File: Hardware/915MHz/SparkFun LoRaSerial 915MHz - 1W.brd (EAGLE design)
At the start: 50.8 x 27.4 mm, 94 parts, among them J1 QWIIC_RIGHT_ANGLE, J3 USB C, J4 JTAG, Q1 20V/0.2A/8MHz/1.2Ω/1Vth, Q2 20V/0.2A/8MHz/1.2Ω/1Vth, U2 ATSAMD21G-A, U3 AP2112K-3.3, U4 E19-915M30S, Y1 32.768kHz

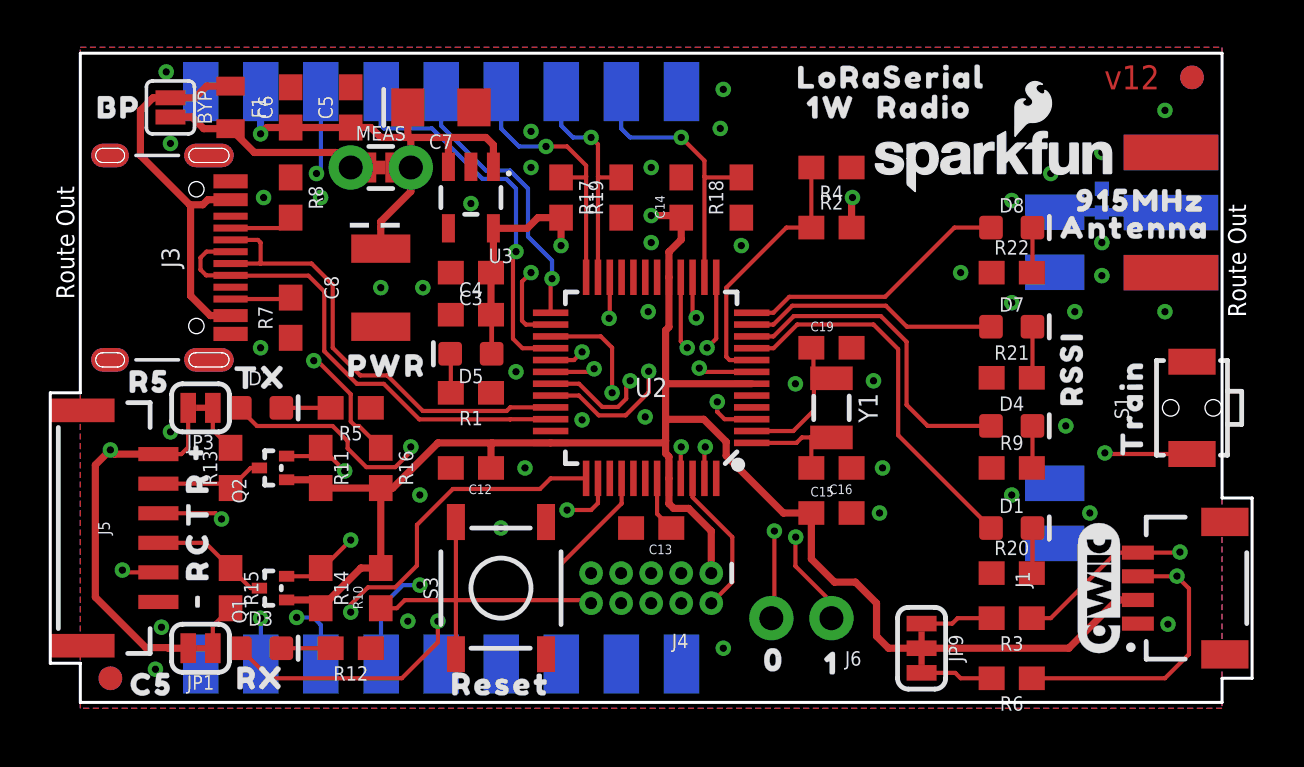
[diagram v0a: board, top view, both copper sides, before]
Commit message: Add RSSI LED drivers. v13
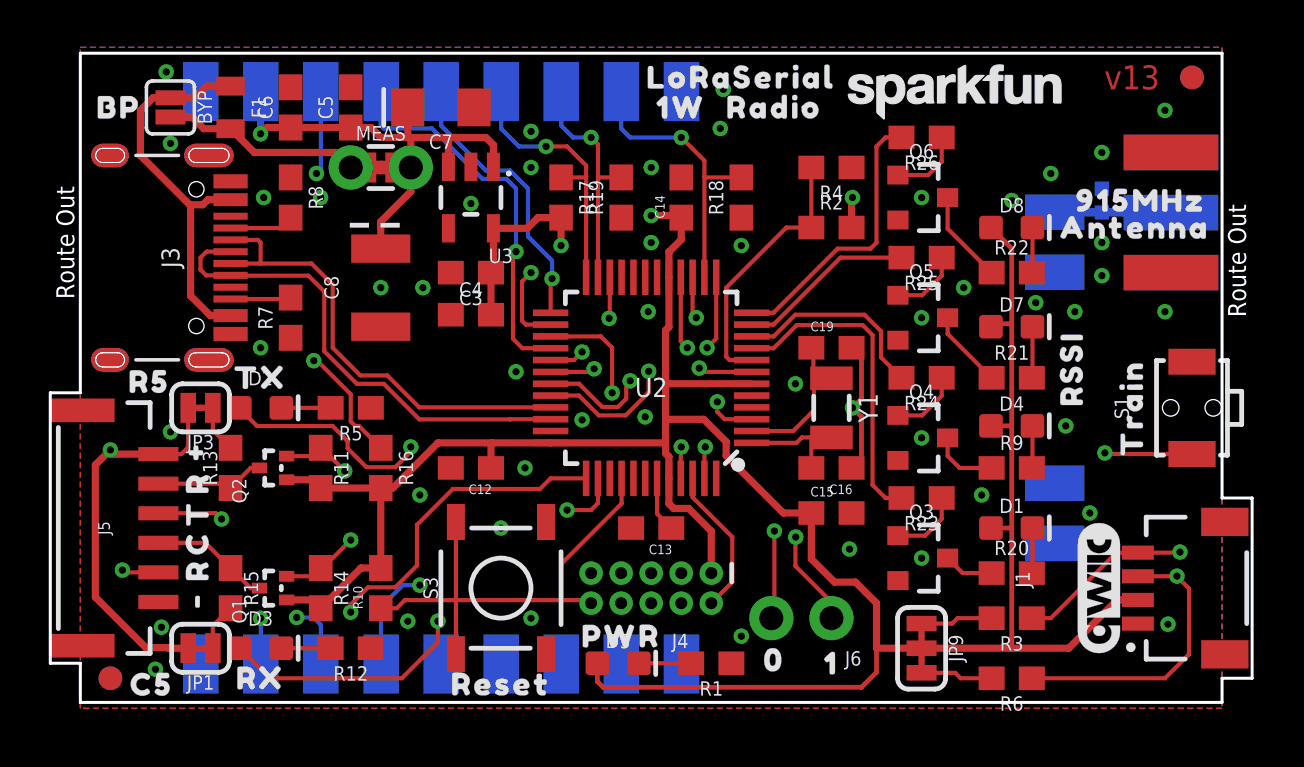
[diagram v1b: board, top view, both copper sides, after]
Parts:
- added Q3, Q4, Q5, Q6: 600mA/40V, SparkFun-DiscreteSemi:SOT23-3
- added R23, R24, R25, R26: 1k, SparkFun-Resistors:0603
- LOGO5: value SFE_LOGO_NAME_FLAME10_MM -> SFE_LOGO_NAME9_MM; device SparkFun-Aesthetics:SFE_LOGO_NAME_FLAME_10MM -> SparkFun-Aesthetics:SFE_LOGO_NAME_9MM
- R20, R21, R22, R9: value 0 -> 220
- U4: device SparkFun-RF:E19-915MS1W -> SparkFun-RF:E19-915M30S
- moved R1 15.3 mm to (27.9, 1.91)
- moved U$7 15.1 mm to (24.1, 3.05)
- moved D5 14.5 mm to (24.0, 1.91), turned to 0 degrees
- moved U$1 6.35 mm to (26.7, 25.4)
- moved U$18 6.35 mm to (29.2, 26.7)
- moved U$5 6.35 mm to (30.6, 25.4)
- moved LOGO5 3.36 mm to (38.2, 26.2)
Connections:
- new net N$12: Q3.3, R20.1
- new net N$13: Q3.1, R23.1
- new net N$14: Q4.3, R9.1
- new net N$15: Q4.1, R24.1
- new net N$16: Q5.3, R21.1
- new net N$17: Q5.1, R25.1
- new net N$18: Q6.3, R22.1
- new net N$19: Q6.1, R26.1
- net 3.3V: now also D1.A, D4.A, D7.A, D8.A
- net A3/RSSI1: now also R23.2; no longer D1.A
- net A4/RSSI2: now also R24.2; no longer D4.A
- net D8/RSSI3: now also R25.2; no longer D7.A
- net D9/RSSI4: now also R26.2; no longer D8.A
- net GND: now also Q3.2, Q4.2, Q5.2, Q6.2; no longer R20.1, R21.1, R22.1, R9.1
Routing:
- net 3.3V: track 98.9 -> 132.3 mm
- net GND: track 0.00 -> 5.74 mm, vias 45 -> 49
- net A4/RSSI2: track 14.0 -> 8.46 mm
- net N$18: track 0.00 -> 3.95 mm
- net N$16: track 0.00 -> 3.31 mm
- net D8/RSSI3: track 10.8 -> 7.50 mm
- net N$19: track 0.00 -> 3.10 mm
- net N$13: track 0.00 -> 3.03 mm
- net N$17: track 0.00 -> 2.95 mm
- net N$15: track 0.00 -> 2.95 mm
- net N$14: track 0.00 -> 2.83 mm
- net A3/RSSI1: track 16.2 -> 13.5 mm
- net N$12: track 0.00 -> 2.12 mm
- net N$7: track 1.66 -> 2.21 mm
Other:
- board text added: "v13"
- board text removed: "v12"

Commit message: Add TPs, GND stitching, sch cosmetic cleanup.
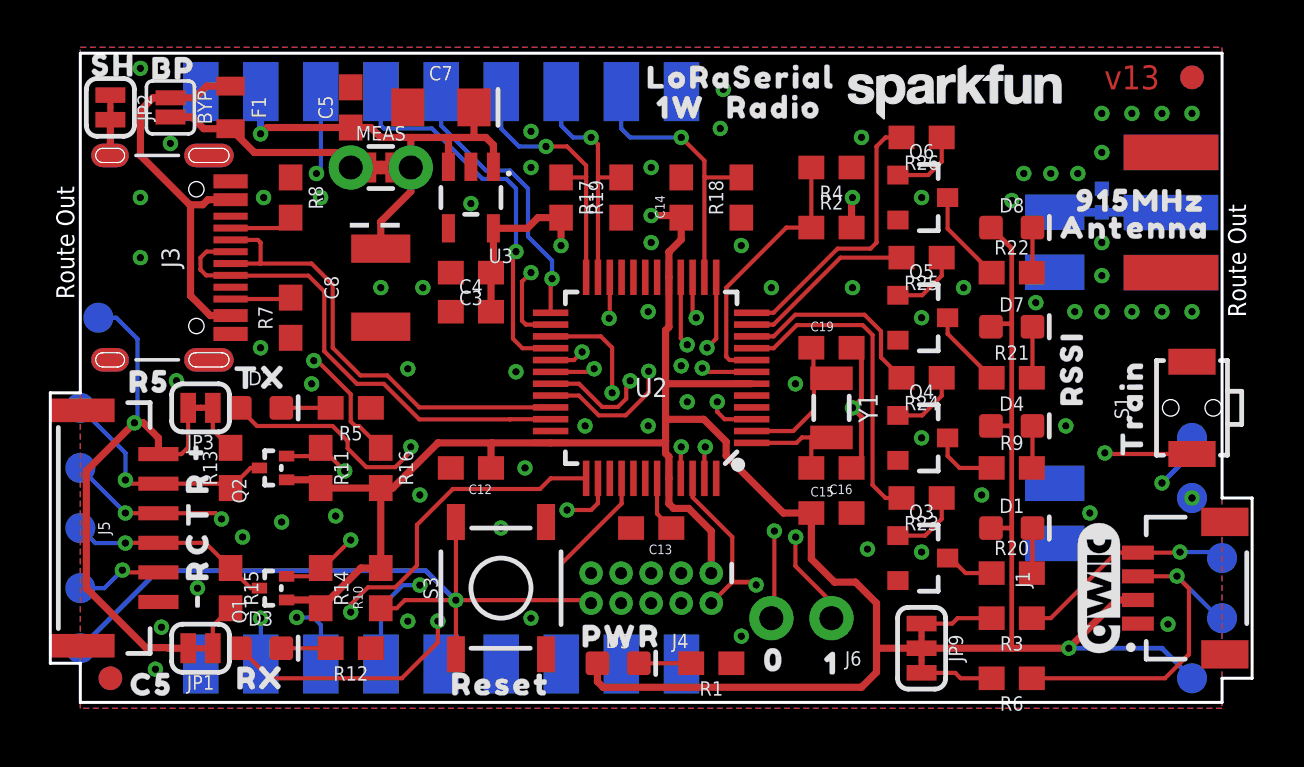
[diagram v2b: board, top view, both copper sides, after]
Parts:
- removed C6: 0.1uF, SparkFun-Capacitors:0603
- added JP2: (no value), SparkFun-Jumpers:SMT-JUMPER_2_NC_TRACE_SILK
- added TP1, TP10, TP11, TP2, TP3, TP4, TP5, TP6, TP7, TP8, TP9: (no value), SparkFun-Connectors:PAD.03X.05
- added U$23: (no value), output:SH0
- C5: value 0.22uF -> 1.0uF
- LOGO2: value SFE_LOGO_NAME_FLAME.1_INCH -> SFE_LOGO_NAME_FLAME9_MM; device SparkFun-Aesthetics:SFE_LOGO_NAME_FLAME_.1 -> SparkFun-Aesthetics:SFE_LOGO_NAME_FLAME_9MM
- moved U$8 2.84 mm to (5.21, 27.1)
- moved LOGO4 1.94 mm to (44.5, 25.4), turned to 90 degrees
- moved C4 0.13 mm to (17.8, 16.8)
- turned C7 to 0 degrees
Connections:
- new net N$20: J3.SHLD1, J3.SHLD2, J3.SHLD3, J3.SHLD4, J3.SHLD5, J3.SHLD6, J3.SHLD7, J3.SHLD8, JP2.2
- net 3.3V: now also TP1.1
- net 5V: now also TP2.1; no longer C6.1
- net CTS-I_HV: now also TP6.1
- net D20/SDA: now also TP10.1
- net D21/SCL: now also TP11.1
- net D38/RTS-O: now also TP9.1
- net GND: now also JP2.1; no longer C6.2
- net RX-I_HV: now also TP7.1
- net SAMD_!RESET!: now also TP5.1
- net SWCLK: now also TP4.1
- net SWDIO: now also TP3.1
- net TX-O: now also TP8.1
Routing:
- net SWDIO: track 6.34 -> 35.2 mm, vias 0 -> 2
- net SWCLK: track 12.5 -> 36.0 mm, vias 1 -> 2
- net SAMD_!RESET!: track 20.9 -> 38.6 mm, vias 0 -> 1
- net 5V: track 59.6 -> 65.6 mm
- net 3.3V: track 132.3 -> 137.9 mm, vias 3 -> 4
- net RX-I_HV: track 4.70 -> 10.00 mm, vias 0 -> 1
- net TX-O: track 31.9 -> 36.0 mm, vias 2 -> 3
- net CTS-I_HV: track 5.06 -> 8.63 mm, vias 0 -> 1
- net D38/RTS-O: track 33.6 -> 36.6 mm
- net D20/SDA: track 45.8 -> 47.7 mm
- net D21/SCL: track 41.5 -> 43.4 mm
- net N$20: track 0.00 -> 1.52 mm
- net GND: vias 49 -> 70

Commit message: v13 - panel files.
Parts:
- removed BYP: JUMPER-SMT_2_NO_SILK, SparkFun-Jumpers:SMT-JUMPER_2_NO_SILK
- removed MEAS: JUMPER-COMBO_2_NC_TRACE, SparkFun-Jumpers:COMBO-JUMPER_2_NC_TRACE
- removed U$8: (no value), output:BP0
- added D9: 3A/10V/280mV, SparkFun-DiscreteSemi:SOD-323
- added Q7: (no value), SparkFun-DiscreteSemi:SOT363_PHILIPS
- added Q8: 20V/4.2A/52mΩ/1.4W, SparkFun-DiscreteSemi:SOT23-3
- added R27: 100k, SparkFun-Resistors:0603
- added R28: 1M, SparkFun-Resistors:0603
- added TP12, TP13: (no value), SparkFun-Connectors:PAD.03X.05
- moved U$11 3.81 mm to (8.89, 10.2)
- moved F1 2.54 mm to (5.08, 25.4)
- moved C8 2.54 mm to (14.0, 20.3)
- moved D2 1.27 mm to (8.89, 11.4)
- moved Q2 1.27 mm to (8.89, 8.89)
- moved R11 1.27 mm to (11.4, 8.89)
- moved R13 1.27 mm to (7.62, 8.89)
- moved R16 1.27 mm to (14.0, 8.89)
- moved R5 1.27 mm to (12.7, 11.4)
- turned R7 to 180 degrees
- turned R8 to 180 degrees
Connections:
- new net N$21: Q7.3, Q8.1, R28.2
- new net N$22: Q7.2, Q7.5, Q7.6, R27.2
- new net VCC_CABLE: J5.1, Q7.1, Q8.3
- net 5V: now also D9.C, Q7.4, Q8.2; no longer J5.1, MEAS.2, MEAS.4
- net A0: now also TP12.1
- net A1: now also TP13.1
- net GND: now also R27.1, R28.1
- net VUSB: no longer BYP.1
- net V_USB: now also D9.A; no longer BYP.2, MEAS.1, MEAS.3
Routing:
- net A0: track 12.2 -> 37.6 mm, vias 2 -> 3
- net A1: track 15.0 -> 35.0 mm, vias 2 -> 3
- net 5V: track 65.6 -> 81.1 mm, vias 2 -> 6
- net VCC_CABLE: track 0.00 -> 13.0 mm
- net V_USB: track 9.27 -> 1.91 mm
- net GND: track 5.74 -> 11.0 mm
- net N$22: track 0.00 -> 4.85 mm
- net N$21: track 0.00 -> 3.40 mm
- net VUSB: track 16.8 -> 14.3 mm
- net TX-O: track 36.0 -> 34.4 mm
- net N$5: track 2.00 -> 3.27 mm
- net D31/TX_LED: track 19.1 -> 17.9 mm
- net D6/LORA_!RST!: track 32.4 -> 33.5 mm, vias 3 -> 4
- net CC2: track 2.56 -> 2.02 mm
- net RX-I_HV: track 10.00 -> 10.5 mm
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
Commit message: Change to in stock 3.3V regulator
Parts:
- U3: value AP2112K-3.3 -> 3.3V/150mA
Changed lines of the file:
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@@
 <layer number="47" name="Measures" color="7" fill="1" visible="no" active="yes"/>
 <layer number="48" name="Document" color="7" fill="1" visible="no" active="yes"/>
-<layer number="49" name="Reference" color="7" fill="1" visible="yes" active="yes"/>
+<layer number="49" name="Reference" color="7" fill="1" visible="no" active="yes"/>
 <layer number="50" name="dxf" color="7" fill="1" visible="no" active="yes"/>
 <layer number="51" name="tDocu" color="6" fill="1" visible="yes" active="yes"/>
@@
 <attribute name="VALUE" x="17.78" y="16.002" size="0.6096" layer="27" font="vector" ratio="20" align="top-center"/>
 </element>
-<element name="U3" library="SparkFun-IC-Power" package="SOT23-5" value="AP2112K-3.3" x="17.78" y="21.59" smashed="yes" rot="R180">
+<element name="U3" library="SparkFun-IC-Power" package="SOT23-5" value="3.3V/150mA" x="17.78" y="21.59" smashed="yes" rot="R180">
 <attribute name="NAME" x="19.558" y="19.431" size="0.6096" layer="25" ratio="20" rot="R180"/>
-<attribute name="PROD_ID" value="VREG-12457" x="22.78" y="21.59" size="1.778" layer="27" font="vector" ratio="15" rot="R180" display="off"/>
-<attribute name="VALUE" x="19.558" y="24.384" size="0.6096" layer="27" ratio="20" rot="R180"/>
+<attribute name="PROD_ID" value="VREG-00822" x="22.78" y="21.59" size="1.778" layer="27" font="vector" ratio="15" rot="R180" display="off"/>
+<attribute name="VALUE" value="3.3V/150mA" x="19.558" y="24.384" size="0.6096" layer="27" ratio="20" rot="R180"/>
 </element>
 <element name="LOGO2" library="SparkFun-Aesthetics" package="SFE_LOGO_NAME_FLAME_9MM" value="SFE_LOGO_NAME_FLAME9_MM" x="44.958" y="6.096" smashed="yes" rot="MR90"/>

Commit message: Change RSSI LED resistors to 22 ohm
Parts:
- R20, R21, R22, R9: value 220 -> 22Ω
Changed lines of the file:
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@@
 <attribute name="VALUE" x="27.94" y="2.667" size="0.6096" layer="27" font="vector" ratio="20" rot="R180" align="top-center"/>
 </element>
-<element name="R9" library="SparkFun-Resistors" package="0603" value="220" x="40.64" y="10.16" smashed="yes">
+<element name="R9" library="SparkFun-Resistors" package="0603" value="22Ω" x="40.64" y="10.16" smashed="yes">
 <attribute name="NAME" x="40.64" y="10.922" size="0.6096" layer="25" font="vector" ratio="20" align="bottom-center"/>
-<attribute name="PROD_ID" value="RES-07861" x="40.64" y="10.16" size="1.778" layer="27" font="vector" ratio="15" display="off"/>
-<attribute name="VALUE" value="220" x="40.64" y="9.398" size="0.6096" layer="27" font="vector" ratio="20" align="top-center"/>
+<attribute name="PROD_ID" value="RES-08698" x="40.64" y="10.16" size="1.778" layer="27" font="vector" ratio="15" display="off"/>
+<attribute name="VALUE" value="22Ω" x="40.64" y="9.398" size="0.6096" layer="27" font="vector" ratio="20" align="top-center"/>
 </element>
 <element name="U$10" library="output" package="RX1" value="" x="8.89" y="1.27" smashed="yes"/>
@@
 <element name="U$19" library="output" package="C50" value="" x="4.3" y="1" smashed="yes"/>
 <element name="U$20" library="output" package="R50" value="" x="4.2" y="13.8" smashed="yes"/>
-<element name="R20" library="SparkFun-Resistors" package="0603" value="220" x="40.64" y="5.715" smashed="yes">
+<element name="R20" library="SparkFun-Resistors" package="0603" value="22Ω" x="40.64" y="5.715" smashed="yes">
 <attribute name="NAME" x="40.64" y="6.477" size="0.6096" layer="25" font="vector" ratio="20" align="bottom-center"/>
-<attribute name="PROD_ID" value="RES-07861" x="41.91" y="5.715" size="1.778" layer="27" font="vector" ratio="15" display="off"/>
-<attribute name="VALUE" value="220" x="40.64" y="4.953" size="0.6096" layer="27" font="vector" ratio="20" align="top-center"/>
+<attribute name="PROD_ID" value="RES-08698" x="41.91" y="5.715" size="1.778" layer="27" font="vector" ratio="15" display="off"/>
+<attribute name="VALUE" value="22Ω" x="40.64" y="4.953" size="0.6096" layer="27" font="vector" ratio="20" align="top-center"/>
 </element>
 <element name="D1" library="SparkFun-LED" package="LED-0603" value="GREEN" x="40.64" y="7.62" smashed="yes">
@@
 <attribute name="VALUE" x="40.64" y="6.985" size="0.6096" layer="27" font="vector" ratio="20" align="top-center"/>
 </element>
-<element name="R21" library="SparkFun-Resistors" package="0603" value="220" x="40.64" y="13.97" smashed="yes">
+<element name="R21" library="SparkFun-Resistors" package="0603" value="22Ω" x="40.64" y="13.97" smashed="yes">
 <attribute name="NAME" x="40.64" y="14.732" size="0.6096" layer="25" font="vector" ratio="20" align="bottom-center"/>
-<attribute name="PROD_ID" value="RES-07861" x="41.91" y="13.97" size="1.778" layer="27" font="vector" ratio="15" display="off"/>
-<attribute name="VALUE" value="220" x="40.64" y="13.208" size="0.6096" layer="27" font="vector" ratio="20" align="top-center"/>
+<attribute name="PROD_ID" value="RES-08698" x="41.91" y="13.97" size="1.778" layer="27" font="vector" ratio="15" display="off"/>
+<attribute name="VALUE" value="22Ω" x="40.64" y="13.208" size="0.6096" layer="27" font="vector" ratio="20" align="top-center"/>
 </element>
 <element name="D7" library="SparkFun-LED" package="LED-0603" value="GREEN" x="40.64" y="16.129" smashed="yes">
@@
 <attribute name="VALUE" x="40.64" y="19.685" size="0.6096" layer="27" font="vector" ratio="20" align="top-center"/>
 </element>
-<element name="R22" library="SparkFun-Resistors" package="0603" value="220" x="40.64" y="18.415" smashed="yes">
+<element name="R22" library="SparkFun-Resistors" package="0603" value="22Ω" x="40.64" y="18.415" smashed="yes">
 <attribute name="NAME" x="40.64" y="19.177" size="0.6096" layer="25" font="vector" ratio="20" align="bottom-center"/>
-<attribute name="PROD_ID" value="RES-07861" x="41.91" y="14.605" size="1.778" layer="27" font="vector" ratio="15" display="off"/>
-<attribute name="VALUE" value="220" x="40.64" y="17.653" size="0.6096" layer="27" font="vector" ratio="20" align="top-center"/>
+<attribute name="PROD_ID" value="RES-08698" x="41.91" y="14.605" size="1.778" layer="27" font="vector" ratio="15" display="off"/>
+<attribute name="VALUE" value="22Ω" x="40.64" y="17.653" size="0.6096" layer="27" font="vector" ratio="20" align="top-center"/>
 </element>
 <element name="U$21" library="output" package="RSSI0" value="" x="43.18" y="14.351" smashed="yes" rot="R90"/>

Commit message: Update schematics with flow control notes
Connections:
- net CTS-I_HV renamed !CTS!-I_HV
- net D30/CTS-I_LV renamed D30/!CTS!-I_LV
- net D38/RTS-O renamed D38/!RTS!-O
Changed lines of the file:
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@@
 <wire x1="26.1239" y1="11.6459" x2="18.161" y2="3.683" width="0.1778" layer="2"/>
 </signal>
-<signal name="D30/CTS-I_LV">
+<signal name="D30/!CTS!-I_LV">
 <contactref element="U2" pad="37"/>
 <contactref element="R14" pad="1"/>
@@
 <contactref element="U2" pad="21"/>
 </signal>
-<signal name="D38/RTS-O">
+<signal name="D38/!RTS!-O">
 <contactref element="U2" pad="22"/>
 <contactref element="J5" pad="5"/>
@@
 <wire x1="3.175" y1="10.795" x2="3.175" y2="9.652" width="0.1778" layer="16"/>
 </signal>
-<signal name="CTS-I_HV">
+<signal name="!CTS!-I_HV">
 <contactref element="J5" pad="4"/>
 <contactref element="Q1" pad="3"/>
